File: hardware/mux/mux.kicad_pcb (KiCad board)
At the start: 2 copper layers, 21.5 x 26.5 mm, 8 parts, among them J1 Left, J2 Right, U1 TMUX6209

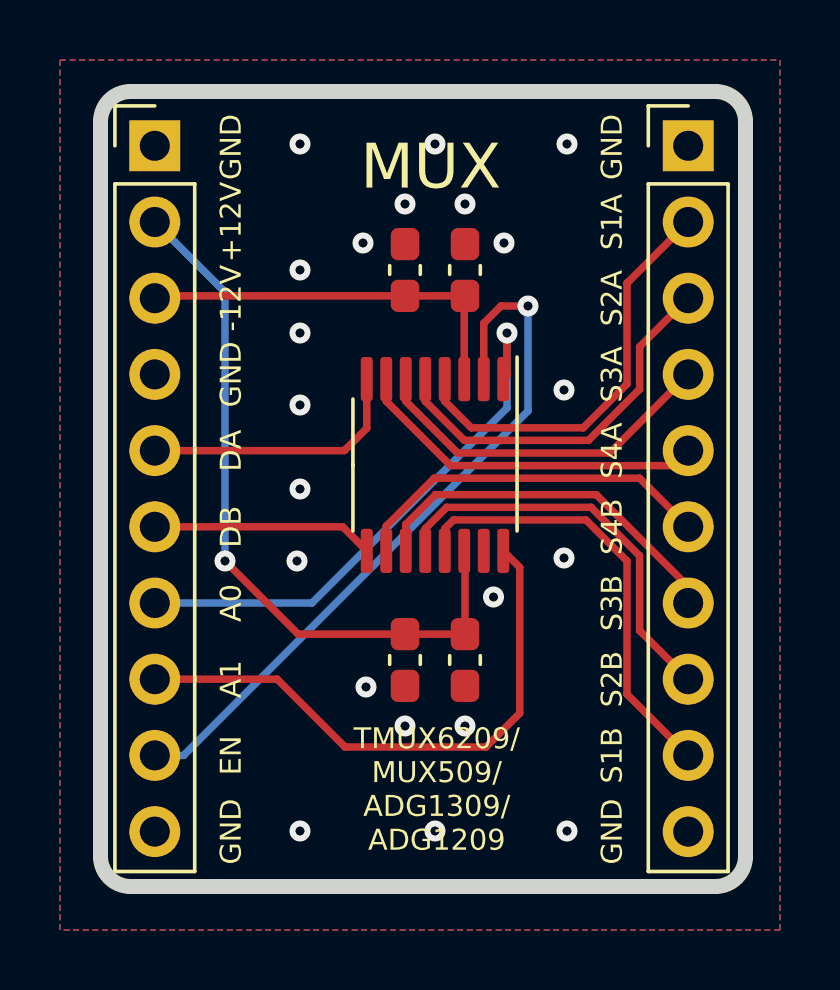
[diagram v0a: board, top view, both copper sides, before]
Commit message: Add pull-ups
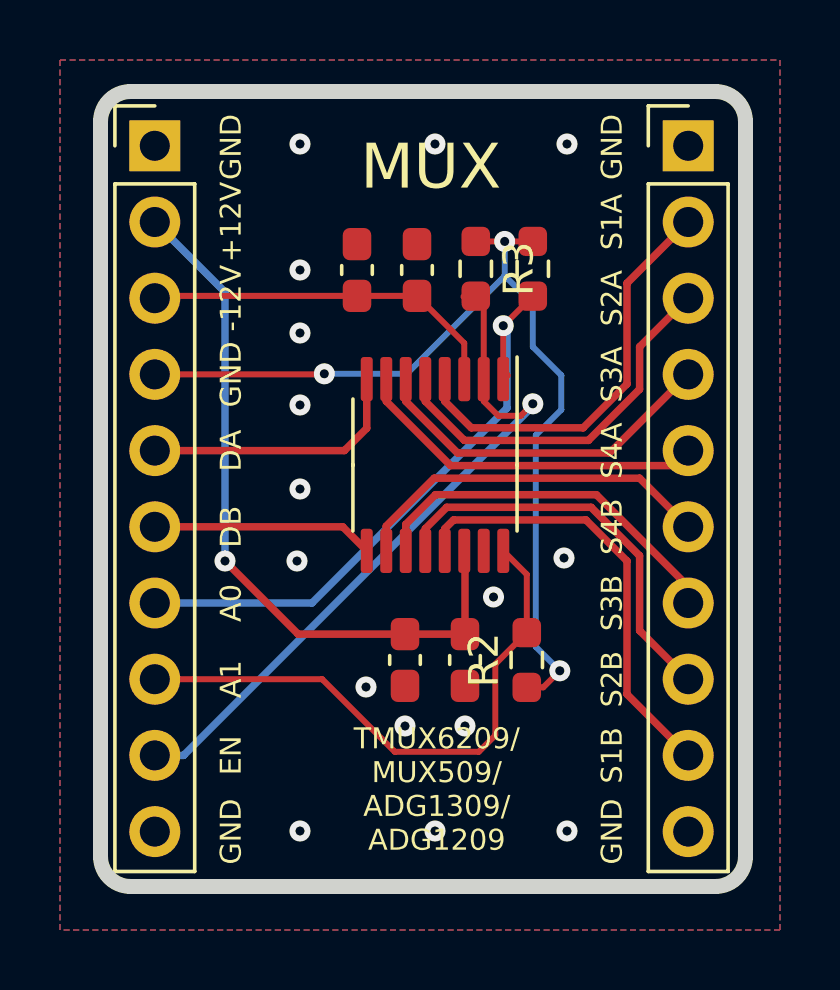
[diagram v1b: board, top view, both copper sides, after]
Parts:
- added R1: 10k, Resistor_SMD:R_0603_1608Metric_Pad0.98x0.95mm_HandSolder, F.Cu at (149.8, 90.5)
- added R2: 10k, Resistor_SMD:R_0603_1608Metric_Pad0.98x0.95mm_HandSolder, F.Cu at (149.6, 103.5)
- added R3: 10k, Resistor_SMD:R_0603_1608Metric_Pad0.98x0.95mm_HandSolder, F.Cu at (147.9, 90.5)
- moved C3 1.60 mm to (143.9, 90.5)
- moved C4 1.60 mm to (145.9, 90.5)
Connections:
- J1 pad 4: GND -> +3V3
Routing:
- net +3V3: track 0.00 -> 32.0 mm, vias 0 -> 3
- net /A0: track 18.5 -> 20.6 mm
- net /EN: track 24.3 -> 23.2 mm
- net -12V: track 13.2 -> 12.2 mm
- net GND: vias 18 -> 13
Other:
- board text added: "Dual 4:1 Analog Multiplexer v1 10/21/2021 CERN-OHL-P V2 testkit.wntr.dev"
- board text removed: "Dual 4:1 Analog Multiplexer v0 10/5/2021 CERN-OHL-P V2 testkit.wntr.dev"
